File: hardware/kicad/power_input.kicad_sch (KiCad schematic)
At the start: 27 parts, among them J301 USB-C power, U301 LP5907MFX-3.3, U302 LP5907MFX-3.3

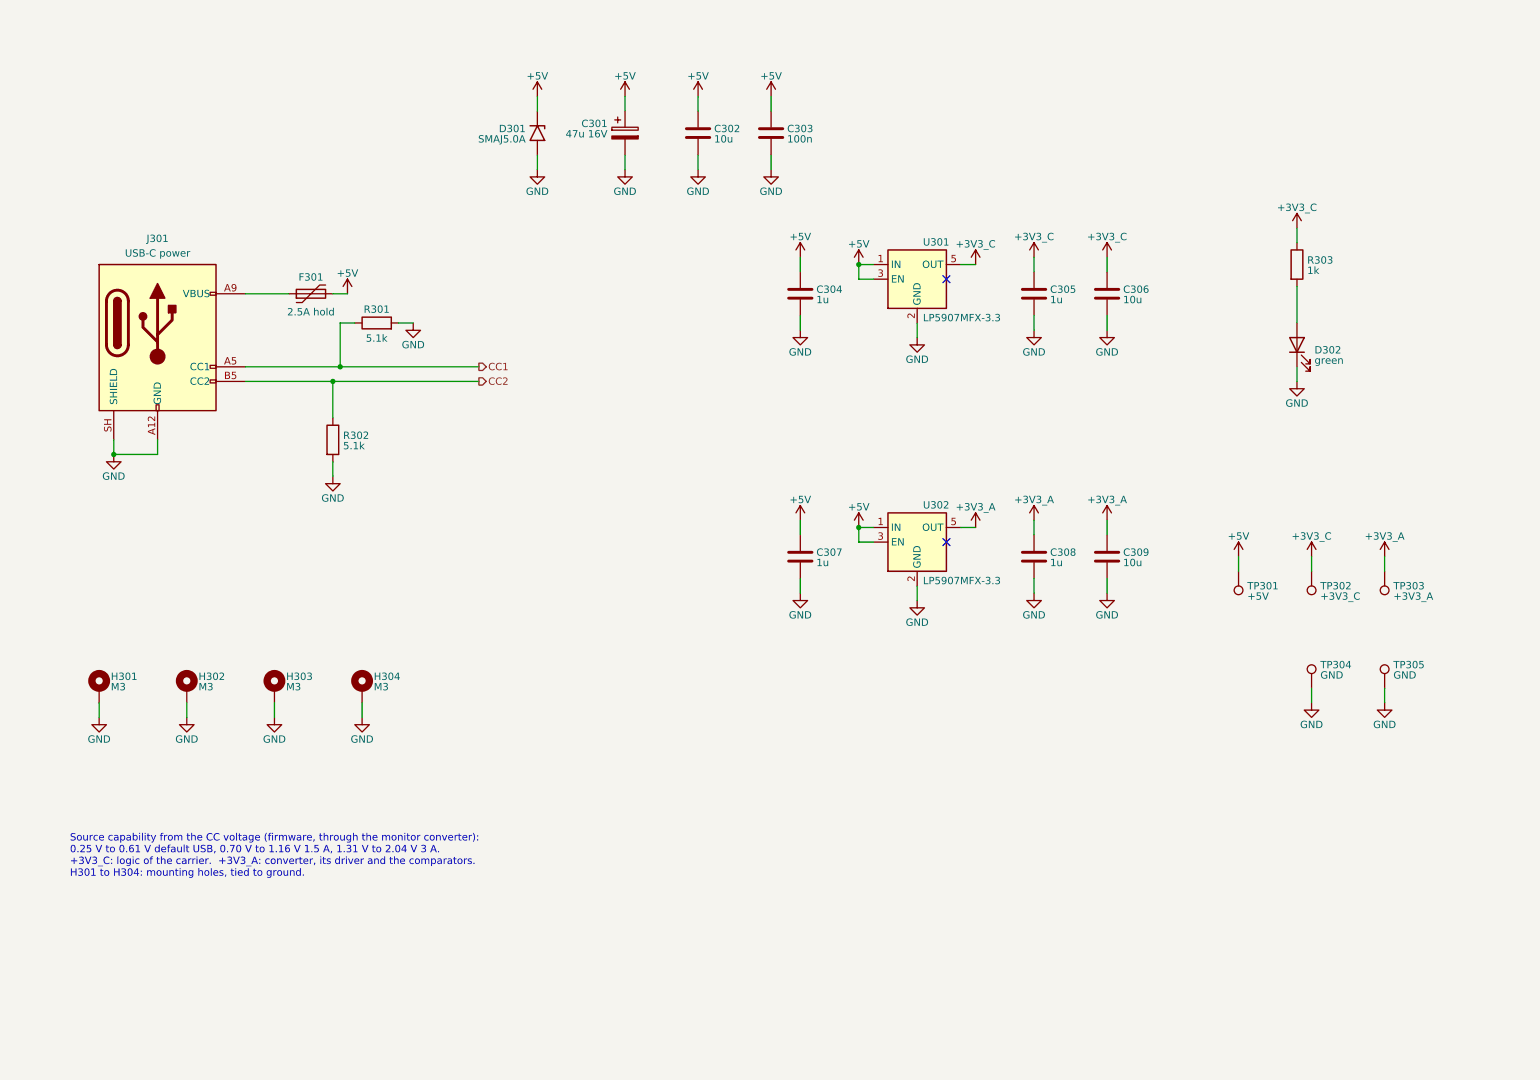
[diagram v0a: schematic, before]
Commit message: feat(hardware)!: draw draft A1 of the schematic around a Pico 2
A Raspberry Pi Pico 2 on two 1x20 sockets replaces the ESP32-S3
development board, the programmable logic device and the buffer
between the two boards (D-39 to D-43 of the specification). The former
interface and range logic sheets become two new ones:

- Controller: the Pico 2, the diodes that join its USB supply and the
  5 V rail of the carrier, resistor arrays in the SPI and acquisition
  lines, a reset button and a console header.
- Side Data: two shift registers that take the range, the status
  signals and the eight logic inputs with every sample.

The DUT connects through a 1x4 pin header and a lever terminal block
in parallel, both GND, VIN, VOUT, GND, and the logic port is a 1x10
header with VCC, GND, D7 to D0: the pin order of the PPK2 (D-44). A
solder jumper selects the supply of the DUT side of the level
translator. A transistor at the driver of the ampere switch holds it
open while VIN is above 5.5 V.

Reference designators are numbered as the annotation tool of KiCad
does by default (D-45). The numbering touches every sheet, so these
changes come in one commit. The symbol and the socket footprint of
the ESP32-S3 board leave the project library; the Pico 2 uses the
symbol and the footprint of the KiCad library.

The electrical rules check reports no errors and no warnings. The
parts stay candidates, and no program for the PIO blocks exists yet.

BREAKING CHANGE: the pins of the controller follow the new pin map of
section 5 of the specification.
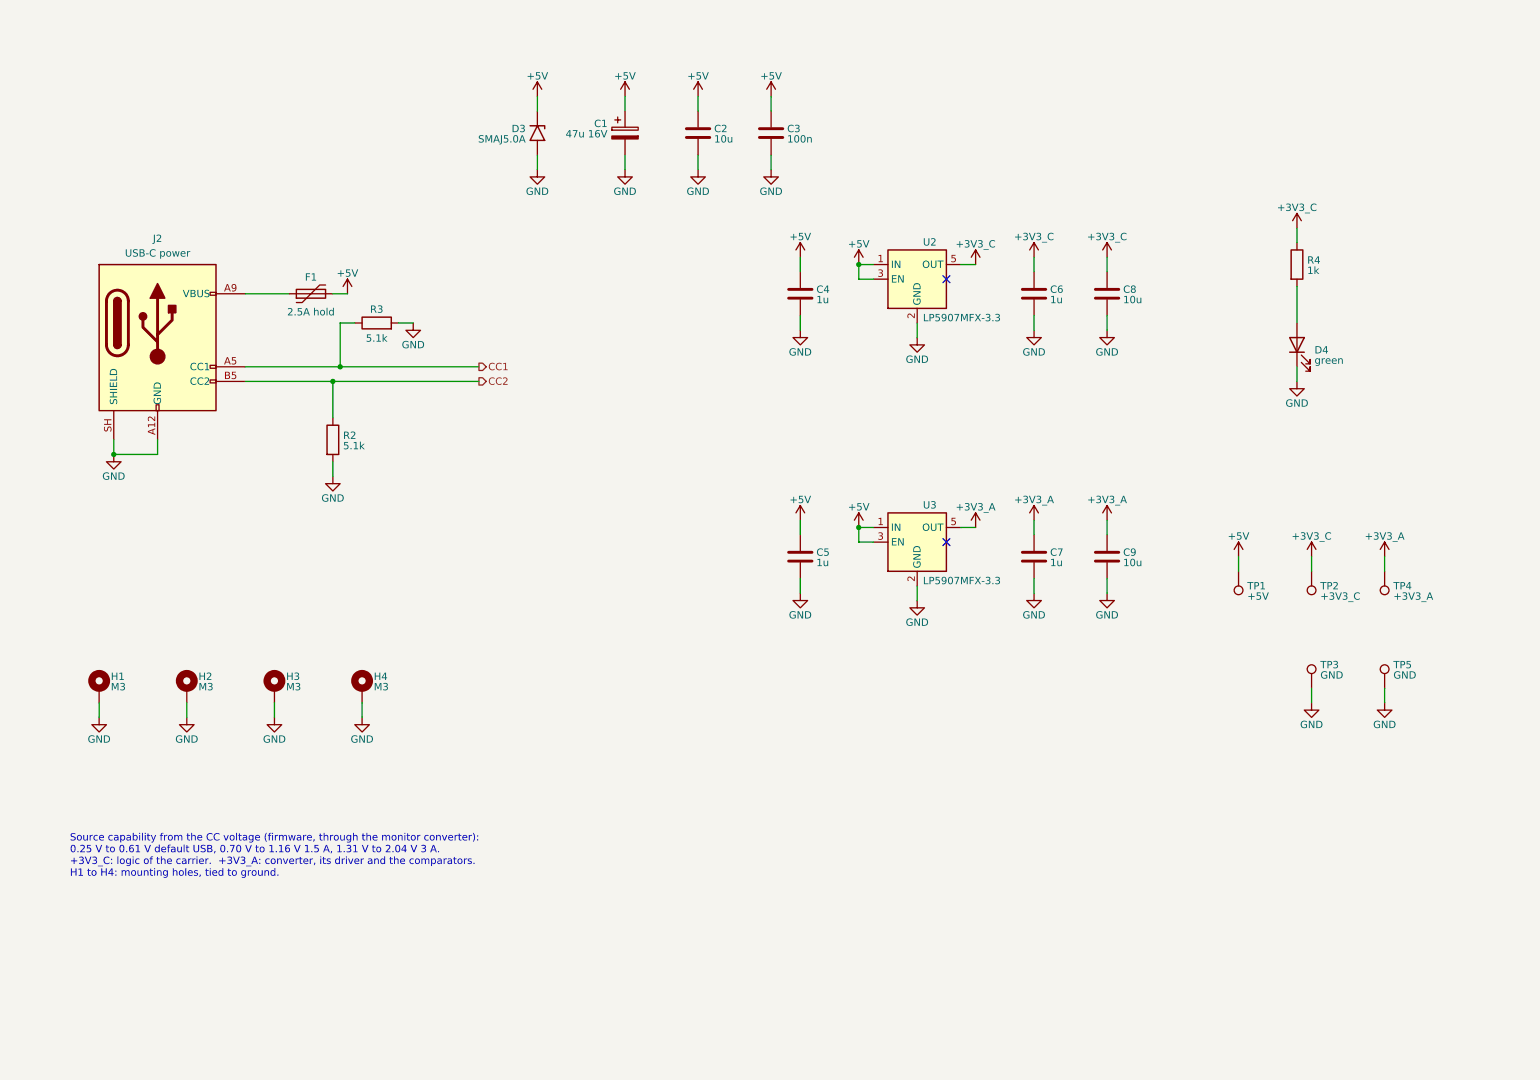
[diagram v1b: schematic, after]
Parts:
- renumbered C301 to C1, C302 to C2, C303 to C3, C304 to C4, C307 to C5, C305 to C6, C308 to C7, C306 to C8, C309 to C9, D301 to D3, D302 to D4, F301 to F1, H301 to H1, H302 to H2, H303 to H3, H304 to H4, J301 to J2, R302 to R2, R301 to R3, R303 to R4, TP301 to TP1, TP302 to TP2, TP304 to TP3, TP303 to TP4, TP305 to TP5, U301 to U2, U302 to U3
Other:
- note added: "Source capability from the CC voltage (firmware, through the monitor converter): 0.25 V to 0.61 V default USB, 0.70 V to 1.16 V 1.5 A, 1.31 V to 2.04 V 3 A. +3V3_C: logic of the carrier. +3V3_A: converter, its driver and the comparators. H1 to H4: mounting holes, tied to ground."
- note removed: "Source capability from the CC voltage (firmware, through the monitor converter): 0.25 V to 0.61 V default USB, 0.70 V to 1.16 V 1.5 A, 1.31 V to 2.04 V 3 A. +3V3_C: logic of the carrier. +3V3_A: converter, its driver and the comparators. H301 to H304: mounting holes, tied to ground."

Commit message: feat(hardware): draw draft A2 of the schematic
428 parts on 15 A4 pages, 14 sheets below the root sheet (D-83). Two
sheets are new: Logic Supplies, with the supervisor of the 5 V rail and
the two 3.3 V regulators, and Rail Monitor, with the comparators behind
PWR_GOOD.

The drawings follow the specification of draft A2: a current limiter
on each supply input and a priority multiplexer, a pre-regulator that
tracks the output of the linear regulator, a VIN path that withstands
-20 V to +20 V with its switch open, two diode-connected MOSFETs as
ladder clamp, thin-film and four-terminal shunts, ESD arrays at the CC
pins and at the VCC pin of the logic port. The reference designators
are numbered as KiCad numbers them (D-45), so they are not those of
draft A1.

The project library gains the symbol of the input multiplexer and two
footprints: the lever terminal block with pads of 1.9 mm x 2.3 mm and
the controller module without its antenna keep-out (D-85).

The electrical rules check reports no errors and no warnings. The
parts are candidates, and nothing is built or measured.
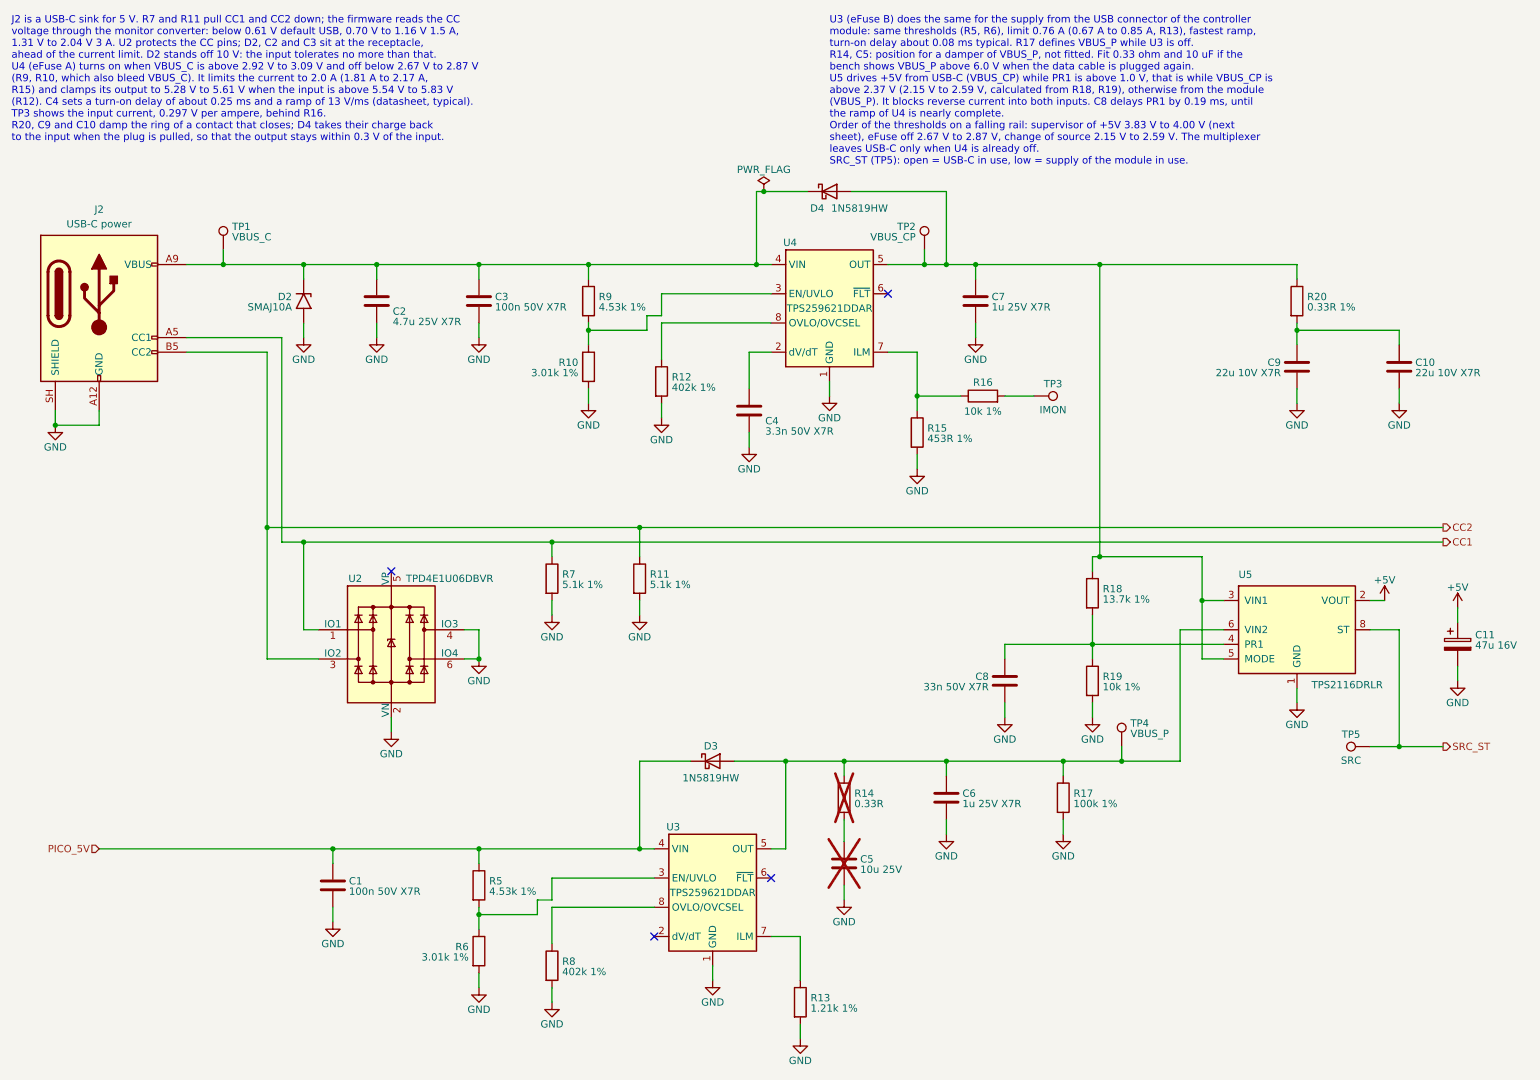
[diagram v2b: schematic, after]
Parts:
- removed D4: green, LED_SMD:LED_0603_1608Metric, symbol Device:LED
- removed F1: 2.5A hold, Fuse:Fuse_1812_4532Metric, symbol Device:Polyfuse
- removed H1, H2, H3, H4: M3, MountingHole:MountingHole_3.2mm_M3_Pad, symbol Mechanical:MountingHole_Pad
- removed R4: 1k, Resistor_SMD:R_0603_1608Metric, symbol Device:R
- removed U2, U3: LP5907MFX-3.3, Package_TO_SOT_SMD:SOT-23-5, symbol Regulator_Linear:LP5907MFX-3.3
- added C1: 100n 50V X7R, Capacitor_SMD:C_0603_1608Metric, symbol Device:C
- added C10: 22u 10V X7R, Capacitor_SMD:C_1206_3216Metric, symbol Device:C
- added D3, D4: 1N5819HW, Diode_SMD:D_SOD-123, symbol Device:D_Schottky
- added R10, R6: 3.01k 1%, Resistor_SMD:R_0603_1608Metric, symbol Device:R
- added R12, R8: 402k 1%, Resistor_SMD:R_0603_1608Metric, symbol Device:R
- added R13: 1.21k 1%, Resistor_SMD:R_0603_1608Metric, symbol Device:R
- added R14: 0.33R, Resistor_SMD:R_0805_2012Metric, symbol Device:R
- added R15: 453R 1%, Resistor_SMD:R_0603_1608Metric, symbol Device:R
- added R16, R19: 10k 1%, Resistor_SMD:R_0603_1608Metric, symbol Device:R
- added R17: 100k 1%, Resistor_SMD:R_0603_1608Metric, symbol Device:R
- added R18: 13.7k 1%, Resistor_SMD:R_0603_1608Metric, symbol Device:R
- added R20: 0.33R 1%, Resistor_SMD:R_0805_2012Metric, symbol Device:R
- added R5, R9: 4.53k 1%, Resistor_SMD:R_0603_1608Metric, symbol Device:R
- added U2: TPD4E1U06DBVR, Package_TO_SOT_SMD:SOT-23-6, symbol Power_Protection:SRV05-4
- added U3, U4: TPS259621DDAR, Package_SO:TI_SO-PowerPAD-8_ThermalVias, symbol Power_Management:TPS2596xx
- added U5: TPS2116DRLR, Package_TO_SOT_SMD:SOT-583-8, symbol PowerProfiler:TPS2116DRL
- C11: renamed from C1; MPN (none) -> 865060343004; Manufacturer (none) -> Wurth Elektronik
- C2: value 10u -> 4.7u 25V X7R; MPN (none) -> CL21B475KAFNNNE; Manufacturer (none) -> Samsung Electro-Mechanics
- C3: value 100n -> 100n 50V X7R; MPN (none) -> C0603C104K5RACTU; Manufacturer (none) -> KEMET
- C4: value 1u -> 3.3n 50V X7R; MPN (none) -> CL10B332KB8NNNC; Manufacturer (none) -> Samsung Electro-Mechanics
- C5: value 1u -> 10u 25V; footprint Capacitor_SMD:C_0603_1608Metric -> Capacitor_SMD:C_0805_2012Metric; now not fitted; now left out of the parts list
- C6, C7: value 1u -> 1u 25V X7R; MPN (none) -> C0603C105K3RACTU; Manufacturer (none) -> KEMET
- C8: value 10u -> 33n 50V X7R; footprint Capacitor_SMD:C_0805_2012Metric -> Capacitor_SMD:C_0603_1608Metric; MPN (none) -> CL10B333KB8NNNC; Manufacturer (none) -> Samsung Electro-Mechanics
- C9: value 10u -> 22u 10V X7R; footprint Capacitor_SMD:C_0805_2012Metric -> Capacitor_SMD:C_1206_3216Metric; MPN (none) -> CL31B226KPHNNNE; Manufacturer (none) -> Samsung Electro-Mechanics
- D2: renamed from D3; value SMAJ5.0A -> SMAJ10A; symbol Diode:SMAJ5.0A -> Diode:SMAJ10A; MPN (none) -> SMAJ10A-E3/61; Manufacturer (none) -> Vishay
- J2: MPN USB4125-GF-A -> USB4125-GF-A-0190; Manufacturer (none) -> GCT
- R11: renamed from R2; value 5.1k -> 5.1k 1%; MPN (none) -> CRCW06035K10FKEA; Manufacturer (none) -> Vishay
- R7: renamed from R3; value 5.1k -> 5.1k 1%; MPN (none) -> CRCW06035K10FKEA; Manufacturer (none) -> Vishay
- TP1: value +5V -> VBUS_C; now left out of the parts list
- TP2: value +3V3_C -> VBUS_CP; now left out of the parts list
- TP3: value GND -> IMON; now left out of the parts list
- TP4: value +3V3_A -> VBUS_P; now left out of the parts list
- TP5: value GND -> SRC; now left out of the parts list
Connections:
- net +5V: now also U5.2 (VOUT), U5.7 (VOUT); no longer C2.1, C3.1, C4.1, C5.1, D2.1 (A1), TP1.1
- net CC1: now also U2.1 (IO1)
- net CC2: now also U2.3 (IO2)
- net GND: now also C1.2, C10.2, R10.2, R12.2, R13.2, R15.2, R17.2, R19.2, R6.2, R8.2, U2.2 (VN), U2.4 (IO3), U2.6 (IO4), U3.1 (GND), U3.9 (GND), U4.1 (GND), U4.9 (GND), U5.1 (GND); no longer TP3.1, TP5.1
- net at J2.A9 (VBUS), J2.B9 (VBUS): now also C2.1, C3.1, D2.1 (A1), TP1.1, D4.1 (K), R9.1, U4.4 (VIN)
- removed net +3V3_A: C7.1, C9.1, TP4.1
- removed net +3V3_C: C6.1, C8.1, TP2.1
- new net: C5.1, R14.2
- new net: C8.1, R18.2, R19.1, U5.4 (PR1)
- new net: R13.1, U3.7 (ILM)
- new net: R5.2, R6.1, U3.3 (EN/UVLO)
- new net: C6.1, D3.2 (A), R14.1, R17.1, TP4.1, U3.5 (OUT), U5.6 (VIN2)
- new net: R8.1, U3.8 (OVLO/OVCSEL)
- new net: C7.1, D4.2 (A), R18.1, R20.1, TP2.1, U4.5 (OUT), U5.3 (VIN1), U5.5 (MODE)
- new net: C10.1, C9.1, R20.2
- new net: R16.2, TP3.1
- new net: R15.1, R16.1, U4.7 (ILM)
- new net: R12.1, U4.8 (OVLO/OVCSEL)
- new net: R10.1, R9.2, U4.3 (EN/UVLO)
- new net: C4.1, U4.2 (dV/dT)
- new net PICO_5V: C1.1, D3.1 (K), R5.1, U3.4 (VIN)
- new net SRC_ST: TP5.1, U5.8 (ST)
- no-connect marks 2 -> 4
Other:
- note added: "J2 is a USB-C sink for 5 V. R7 and R11 pull CC1 and CC2 down; the firmware reads the CC voltage through the monitor converter: below 0.61 V default USB, 0.70 V to 1.16 V 1.5 A, 1.31 V to 2.04 V 3 A. U2 protects the CC pins; D2, C2 and C3 sit at the receptacle, ahead of the current limit. D2 stands off 10 V: the input tolerates no more than that. U4 (eFuse A) turns on when VBUS_C is above 2.92 V t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"
- note added: "U3 (eFuse B) does the same for the supply from the USB connector of the controller module: same thresholds (R5, R6), limit 0.76 A (0.67 A to 0.85 A, R13), fastest ramp, turn-on delay about 0.08 ms typical. R17 defines VBUS_P while U3 is off. R14, C5: position for a damper of VBUS_P, not fitted. Fit 0.33 ohm and 10 uF if the bench shows VBUS_P above 6.0 V when the data cable is plugged again. U5 d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"
- note removed: "Source capability from the CC voltage (firmware, through the monitor converter): 0.25 V to 0.61 V default USB, 0.70 V to 1.16 V 1.5 A, 1.31 V to 2.04 V 3 A. +3V3_C: logic of the carrier. +3V3_A: converter, its driver and the comparators. H1 to H4: mounting holes, tied to ground."
- title: Power Input and Logic Supplies -> Power Input: USB-C, Current Limits and Source Selection
- moved on the sheet: C11, C2, C3, D2, J2, R11, R7
